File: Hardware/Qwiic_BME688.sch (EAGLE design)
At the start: 24 parts, among them J1 DNP, J2 QWIIC_RA, J4 QWIIC_RA

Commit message: Create BME688 eagle footprint and schematic symbol
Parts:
- added U1: BME688LGA, BME688:BME688LGA
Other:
- note added: "BME688 Gas Sensor"
- note removed: "SGP40"
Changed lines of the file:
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@@
 <part name="JP7" library="SparkFun-Hardware" deviceset="STAND-OFF" device=""/>
 <part name="JP8" library="SparkFun-Hardware" deviceset="STAND-OFF" device=""/>
+<part name="U1" library="BME688" deviceset="BME688" device="LGA"/>
 </parts>
 <sheets>
@@
 <plain>
 <text x="237.744" y="7.366" size="2.54" layer="94" font="vector">v01</text>
-<text x="121.92" y="73.66" size="1.778" layer="97" font="vector" align="center">7-bit unshifted I2C address: 0x59</text>
+<text x="210.82" y="76.2" size="1.778" layer="97" font="vector" align="center">7-bit unshifted I2C address: 0x59</text>
 <text x="61.468" y="144.526" size="1.778" layer="97" font="vector">Power</text>
 <wire x1="0" y1="127" x2="121.92" y2="127" width="0.2032" layer="97" style="longdash"/>
@@
 <wire x1="121.92" y1="127" x2="121.92" y2="185.42" width="0.2032" layer="97" style="longdash"/>
 <text x="144.78" y="177.8" size="2.54" layer="94" font="vector" align="center">I2C Pull-Up</text>
-<text x="12.7" y="119.38" size="2.54" layer="94" font="vector" align="center">SGP40</text>
+<text x="20.32" y="121.92" size="2.54" layer="94" font="vector" align="center">BME688 Gas Sensor</text>
 <text x="20.32" y="60.96" size="2.54" layer="94" font="vector" align="center">Connectors</text>
 <text x="58.42" y="165.1" size="1.778" layer="97" font="vector">Cut the PWR jumper to
@@
 <wire x1="121.92" y1="0" x2="121.92" y2="68.58" width="0.2032" layer="97" style="longdash"/>
 <text x="168.402" y="11.43" size="2.54" layer="94" font="vector">Priyanka Makin</text>
-<text x="121.92" y="78.74" size="1.778" layer="97" font="vector" align="center">Abs min/max Vdd and Vddh: -0.3 to +3.6V
+<text x="205.74" y="81.28" size="1.778" layer="97" font="vector" align="center">Abs min/max Vdd and Vddh: -0.3 to +3.6V
 Operating current @ 3.3V: 3.0 mA</text>
 </plain>
@@
 <instance part="JP7" gate="G$1" x="243.84" y="30.48" smashed="yes"/>
 <instance part="JP8" gate="G$1" x="243.84" y="27.94" smashed="yes"/>
+<instance part="U1" gate="U1" x="58.42" y="99.06" smashed="yes">
+<attribute name="NAME" x="48.26" y="105.156" size="1.778" layer="95" font="vector"/>
+<attribute name="VALUE" x="48.26" y="88.9" size="1.778" layer="96" font="vector"/>
+</instance>
 </instances>
 <busses>

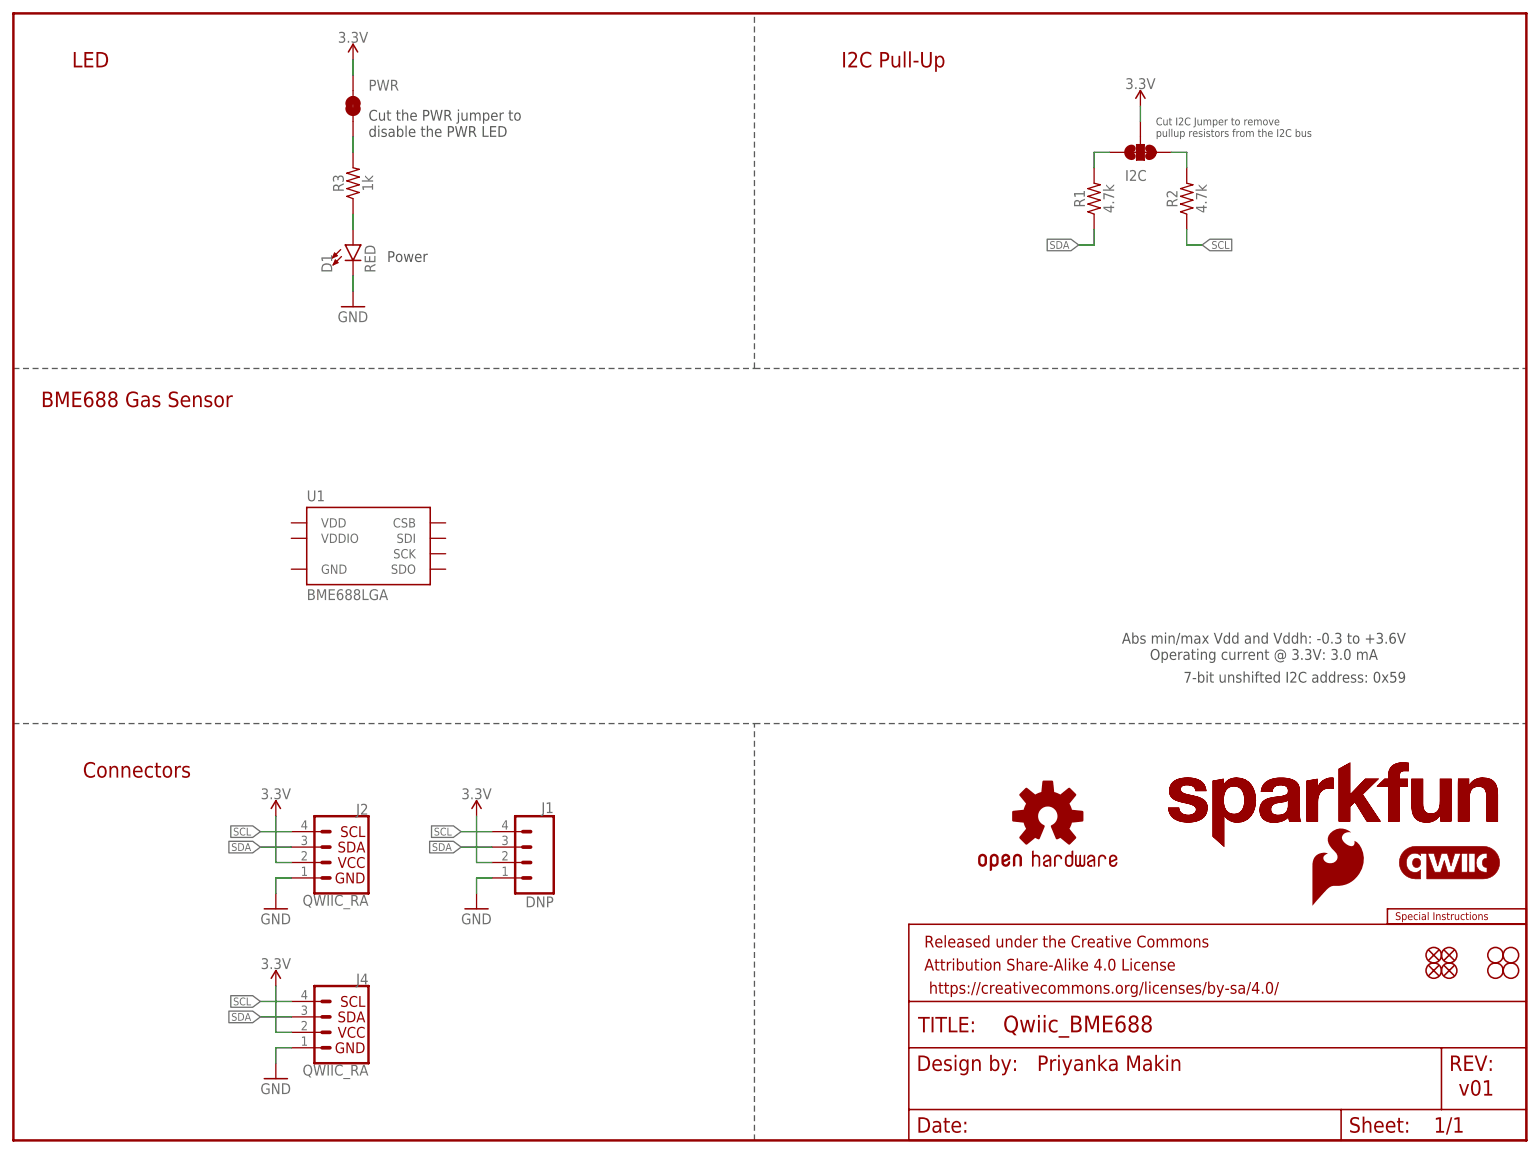
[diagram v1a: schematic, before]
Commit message: Schematic done
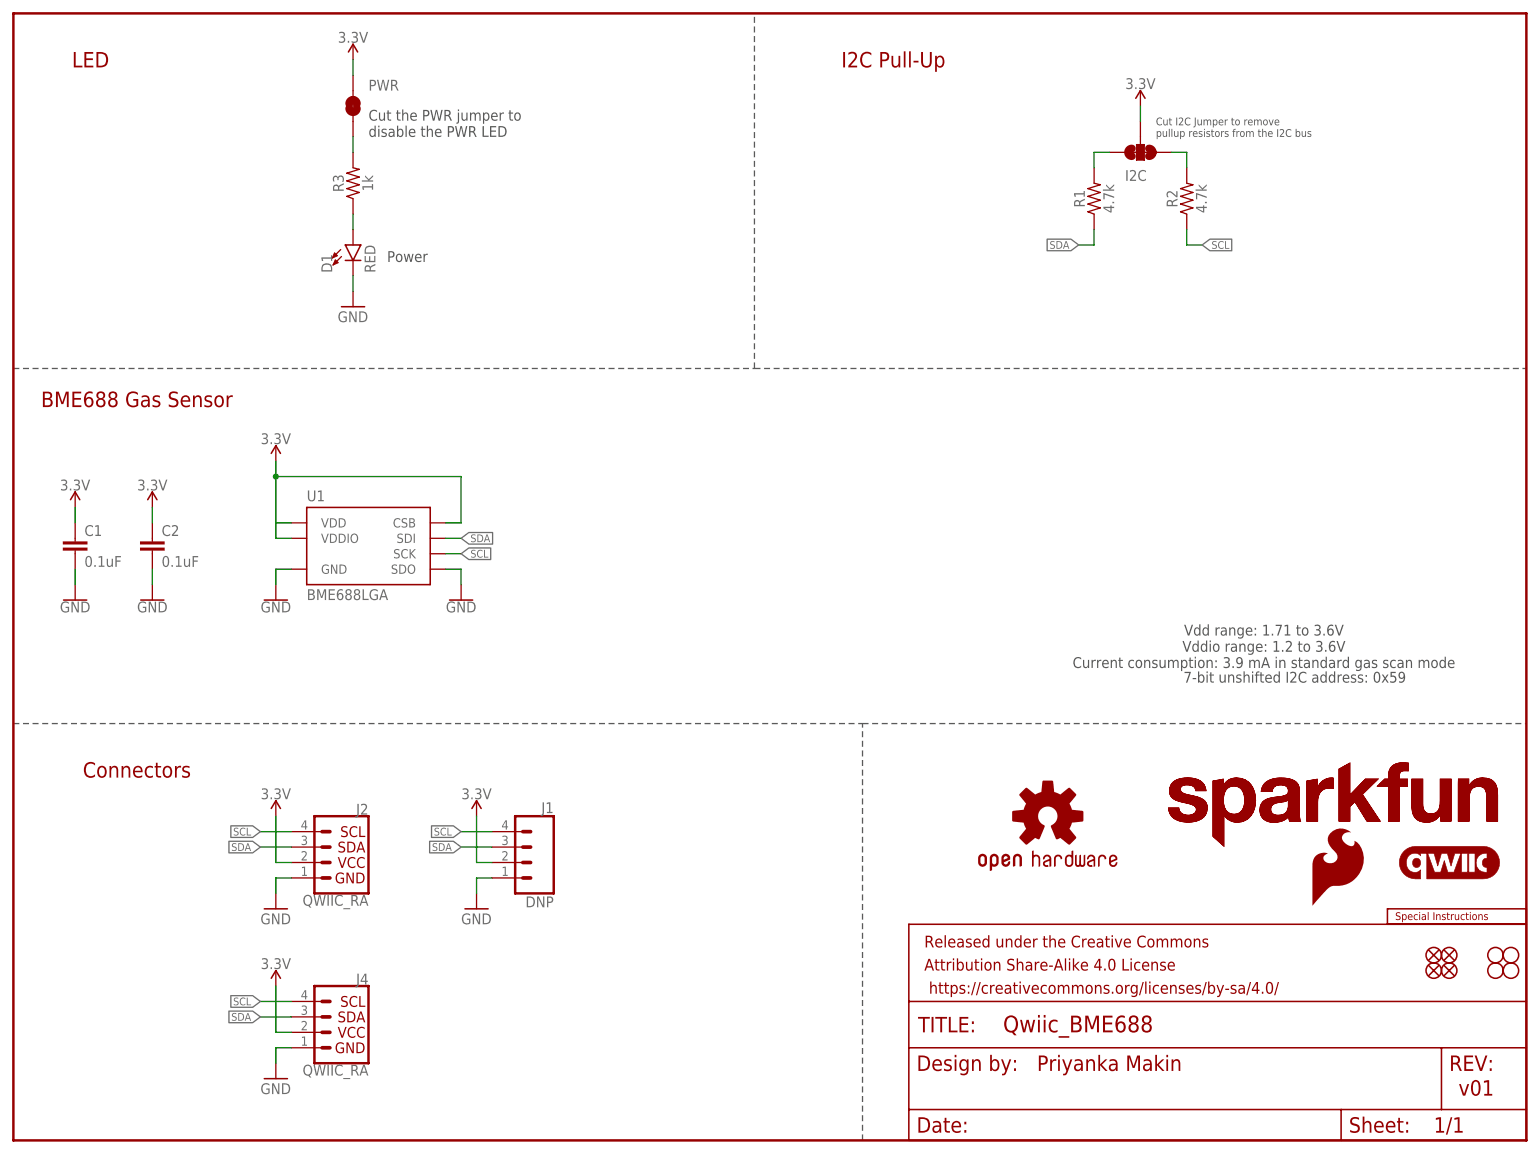
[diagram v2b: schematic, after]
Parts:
- added C1, C2: 0.1uF, SparkFun-Capacitors:0.1UF-0402-16V-10%
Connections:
- net 3.3V: now also C1.1, C2.1, U1.CSB, U1.VDD, U1.VDDIO
- net GND: now also C1.2, C2.2, U1.GND, U1.SDO
- net SCL: now also U1.SCK
- net SDA: now also U1.SDI
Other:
- note added: "Vdd range: 1.71 to 3.6V Vddio range: 1.2 to 3.6V Current consumption: 3.9 mA in standard gas scan mode"
- note removed: "Abs min/max Vdd and Vddh: -0.3 to +3.6V Operating current @ 3.3V: 3.0 mA"
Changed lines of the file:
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@@
 <layer number="56" name="wert" color="7" fill="1" visible="no" active="no"/>
 <layer number="57" name="tCAD" color="7" fill="1" visible="no" active="no"/>
+<layer number="58" name="bCopper" color="7" fill="1" visible="no" active="no"/>
 <layer number="59" name="tCarbon" color="7" fill="1" visible="no" active="no"/>
 <layer number="60" name="bCarbon" color="7" fill="1" visible="no" active="no"/>
@@
 <layer number="250" name="Descript" color="3" fill="1" visible="no" active="no"/>
 <layer number="251" name="SMDround" color="12" fill="11" visible="no" active="no"/>
+<layer number="253" name="Extra" color="7" fill="1" visible="no" active="no"/>
 <layer number="254" name="cooling" color="7" fill="1" visible="yes" active="yes"/>
 <layer number="255" name="routoute" color="7" fill="1" visible="yes" active="yes"/>
@@
 <part name="JP8" library="SparkFun-Hardware" deviceset="STAND-OFF" device=""/>
 <part name="U1" library="BME688" deviceset="BME688" device="LGA"/>
+<part name="GND1" library="SparkFun-PowerSymbols" deviceset="GND" device=""/>
+<part name="GND2" library="SparkFun-PowerSymbols" deviceset="GND" device=""/>
+<part name="SUPPLY1" library="SparkFun-PowerSymbols" deviceset="3.3V" device=""/>
+<part name="C1" library="SparkFun-Capacitors" deviceset="0.1UF" device="-0402-16V-10%" value="0.1uF"/>
+<part name="C2" library="SparkFun-Capacitors" deviceset="0.1UF" device="-0402-16V-10%" value="0.1uF"/>
+<part name="SUPPLY2" library="SparkFun-PowerSymbols" deviceset="3.3V" device=""/>
+<part name="SUPPLY3" library="SparkFun-PowerSymbols" deviceset="3.3V" device=""/>
+<part name="GND4" library="SparkFun-PowerSymbols" deviceset="GND" device=""/>
+<part name="GND5" library="SparkFun-PowerSymbols" deviceset="GND" device=""/>
 </parts>
 <sheets>
@@
 <wire x1="0" y1="127" x2="121.92" y2="127" width="0.2032" layer="97" style="longdash"/>
 <wire x1="121.92" y1="127" x2="248.92" y2="127" width="0.2032" layer="97" style="longdash"/>
-<wire x1="0" y1="68.58" x2="121.92" y2="68.58" width="0.2032" layer="97" style="longdash"/>
-<wire x1="121.92" y1="68.58" x2="248.92" y2="68.58" width="0.2032" layer="97" style="longdash"/>
+<wire x1="0" y1="68.58" x2="139.7" y2="68.58" width="0.2032" layer="97" style="longdash"/>
+<wire x1="139.7" y1="68.58" x2="248.92" y2="68.58" width="0.2032" layer="97" style="longdash"/>
 <wire x1="121.92" y1="127" x2="121.92" y2="185.42" width="0.2032" layer="97" style="longdash"/>
 <text x="144.78" y="177.8" size="2.54" layer="94" font="vector" align="center">I2C Pull-Up</text>
@@
 pullup resistors from the I2C bus</text>
 <text x="12.7" y="177.8" size="2.54" layer="94" font="vector" align="center">LED</text>
-<wire x1="121.92" y1="0" x2="121.92" y2="68.58" width="0.2032" layer="97" style="longdash"/>
+<wire x1="139.7" y1="0" x2="139.7" y2="68.58" width="0.2032" layer="97" style="longdash"/>
 <text x="168.402" y="11.43" size="2.54" layer="94" font="vector">Priyanka Makin</text>
-<text x="205.74" y="81.28" size="1.778" layer="97" font="vector" align="center">Abs min/max Vdd and Vddh: -0.3 to +3.6V
-Operating current @ 3.3V: 3.0 mA</text>
+<text x="205.74" y="81.28" size="1.778" layer="97" font="vector" align="center">Vdd range: 1.71 to 3.6V
+Vddio range: 1.2 to 3.6V
+Current consumption: 3.9 mA in standard gas scan mode</text>
 </plain>
 <instances>
@@
 <attribute name="VALUE" x="48.26" y="88.9" size="1.778" layer="96" font="vector"/>
 </instance>
+<instance part="GND1" gate="1" x="73.66" y="88.9" smashed="yes">
+<attribute name="VALUE" x="73.66" y="88.646" size="1.778" layer="96" align="top-center"/>
+</instance>
+<instance part="GND2" gate="1" x="43.18" y="88.9" smashed="yes">
+<attribute name="VALUE" x="43.18" y="88.646" size="1.778" layer="96" align="top-center"/>
+</instance>
+<instance part="SUPPLY1" gate="G$1" x="43.18" y="111.76" smashed="yes">
+<attribute name="VALUE" x="43.18" y="114.554" size="1.778" layer="96" align="bottom-center"/>
+</instance>
+<instance part="C1" gate="G$1" x="10.16" y="96.52" smashed="yes">
+<attribute name="NAME" x="11.684" y="99.441" size="1.778" layer="95" font="vector"/>
+<attribute name="VALUE" x="11.684" y="94.361" size="1.778" layer="96" font="vector"/>
+</instance>
+<instance part="C2" gate="G$1" x="22.86" y="96.52" smashed="yes">
+<attribute name="NAME" x="24.384" y="99.441" size="1.778" layer="95" font="vector"/>
+<attribute name="VALUE" x="24.384" y="94.361" size="1.778" layer="96" font="vector"/>
+</instance>
+<instance part="SUPPLY2" gate="G$1" x="10.16" y="104.14" smashed="yes">
+<attribute name="VALUE" x="10.16" y="106.934" size="1.778" layer="96" align="bottom-center"/>
+</instance>
+<instance part="SUPPLY3" gate="G$1" x="22.86" y="104.14" smashed="yes">
+<attribute name="VALUE" x="22.86" y="106.934" size="1.778" layer="96" align="bottom-center"/>
+</instance>
+<instance part="GND4" gate="1" x="10.16" y="88.9" smashed="yes">
+<attribute name="VALUE" x="10.16" y="88.646" size="1.778" layer="96" align="top-center"/>
+</instance>
+<instance part="GND5" gate="1" x="22.86" y="88.9" smashed="yes">
+<attribute name="VALUE" x="22.86" y="88.646" size="1.778" layer="96" align="top-center"/>
+</instance>
 </instances>
 <busses>
@@
 <wire x1="185.42" y1="170.18" x2="185.42" y2="167.64" width="0.1524" layer="91"/>
 </segment>
+<segment>
+<pinref part="U1" gate="U1" pin="VDDIO"/>
+<wire x1="45.72" y1="99.06" x2="43.18" y2="99.06" width="0.1524" layer="91"/>
+<wire x1="43.18" y1="99.06" x2="43.18" y2="101.6" width="0.1524" layer="91"/>
+<pinref part="U1" gate="U1" pin="VDD"/>
+<wire x1="43.18" y1="111.76" x2="43.18" y2="109.22" width="0.1524" layer="91"/>
+<wire x1="43.18" y1="109.22" x2="43.18" y2="101.6" width="0.1524" layer="91"/>
+<wire x1="43.18" y1="101.6" x2="45.72" y2="101.6" width="0.1524" layer="91"/>
+<pinref part="U1" gate="U1" pin="CSB"/>
+<wire x1="71.12" y1="101.6" x2="73.66" y2="101.6" width="0.1524" layer="91"/>
+<wire x1="73.66" y1="101.6" x2="73.66" y2="109.22" width="0.1524" layer="91"/>
+<wire x1="73.66" y1="109.22" x2="43.18" y2="109.22" width="0.1524" layer="91"/>
+<junction x="43.18" y="109.22"/>
+<pinref part="SUPPLY1" gate="G$1" pin="3.3V"/>
+</segment>
+<segment>
+<pinref part="C1" gate="G$1" pin="1"/>
+<pinref part="SUPPLY2" gate="G$1" pin="3.3V"/>
+<wire x1="10.16" y1="104.14" x2="10.16" y2="101.6" width="0.1524" layer="91"/>
+</segment>
+<segment>
+<pinref part="C2" gate="G$1" pin="1"/>
+<pinref part="SUPPLY3" gate="G$1" pin="3.3V"/>
+<wire x1="22.86" y1="104.14" x2="22.86" y2="101.6" width="0.1524" layer="91"/>
+</segment>
 </net>
 <net name="GND" class="0">
@@
 <wire x1="55.88" y1="139.7" x2="55.88" y2="142.24" width="0.1524" layer="91"/>
 </segment>
+<segment>
+<pinref part="U1" gate="U1" pin="SDO"/>
+<wire x1="71.12" y1="93.98" x2="73.66" y2="93.98" width="0.1524" layer="91"/>
+<wire x1="73.66" y1="93.98" x2="73.66" y2="91.44" width="0.1524" layer="91"/>
+<pinref part="GND1" gate="1" pin="GND"/>
+</segment>
+<segment>
+<pinref part="U1" gate="U1" pin="GND"/>
+<wire x1="45.72" y1="93.98" x2="43.18" y2="93.98" width="0.1524" layer="91"/>
+<wire x1="43.18" y1="93.98" x2="43.18" y2="91.44" width="0.1524" layer="91"/>
+<pinref part="GND2" gate="1" pin="GND"/>
+</segment>
+<segment>
+<pinref part="C1" gate="G$1" pin="2"/>
+<pinref part="GND4" gate="1" pin="GND"/>
+<wire x1="10.16" y1="91.44" x2="10.16" y2="93.98" width="0.1524" layer="91"/>
+</segment>
+<segment>
+<pinref part="C2" gate="G$1" pin="2"/>
+<pinref part="GND5" gate="1" pin="GND"/>
+<wire x1="22.86" y1="91.44" x2="22.86" y2="93.98" width="0.1524" layer="91"/>
+</segment>
 </net>
 <net name="SCL" class="0">
@@
 <label x="195.58" y="147.32" size="1.27" layer="95" font="vector" xref="yes"/>
 </segment>
+<segment>
+<pinref part="U1" gate="U1" pin="SCK"/>
+<wire x1="71.12" y1="96.52" x2="73.66" y2="96.52" width="0.1524" layer="91"/>
+<label x="73.66" y="96.52" size="1.27" layer="95" xref="yes"/>
+</segment>
 </net>
 <net name="SDA" class="0">
@@
 <label x="175.26" y="147.32" size="1.27" layer="95" font="vector" rot="R180" xref="yes"/>
 </segment>
+<segment>
+<pinref part="U1" gate="U1" pin="SDI"/>
+<wire x1="71.12" y1="99.06" x2="73.66" y2="99.06" width="0.1524" layer="91"/>
+<label x="73.66" y="99.06" size="1.27" layer="95" xref="yes"/>
+</segment>
 </net>

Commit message: Updating schematic
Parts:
- added ADR: JUMPER-SMT_3_1-NC_TRACE_SILK, SparkFun-Jumpers:JUMPER-SMT_3_1-NC_TRACE_SILK
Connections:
- new net N$6: ADR.2, U1.SDO
- net 3.3V: now also ADR.1
- net GND: now also ADR.3; no longer U1.SDO
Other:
- note added: "Cut this jumper and connect to Vddio for I2C address: 0x77"
- note added: "Default, 7-bit unshifted I2C address: 0x76"
- note removed: "7-bit unshifted I2C address: 0x59"
- moved on the sheet: C1, C2, U1
